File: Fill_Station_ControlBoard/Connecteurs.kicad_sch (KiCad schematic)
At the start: 57 parts, among them J3 USB_C_Receptacle_USB2.0_14P, J4 DE9_Pins, J6 RJ45_Wuerth_7499010211A, U2 USBLC6-2SC6, U3 TCAN337G, U5 LAN8742A

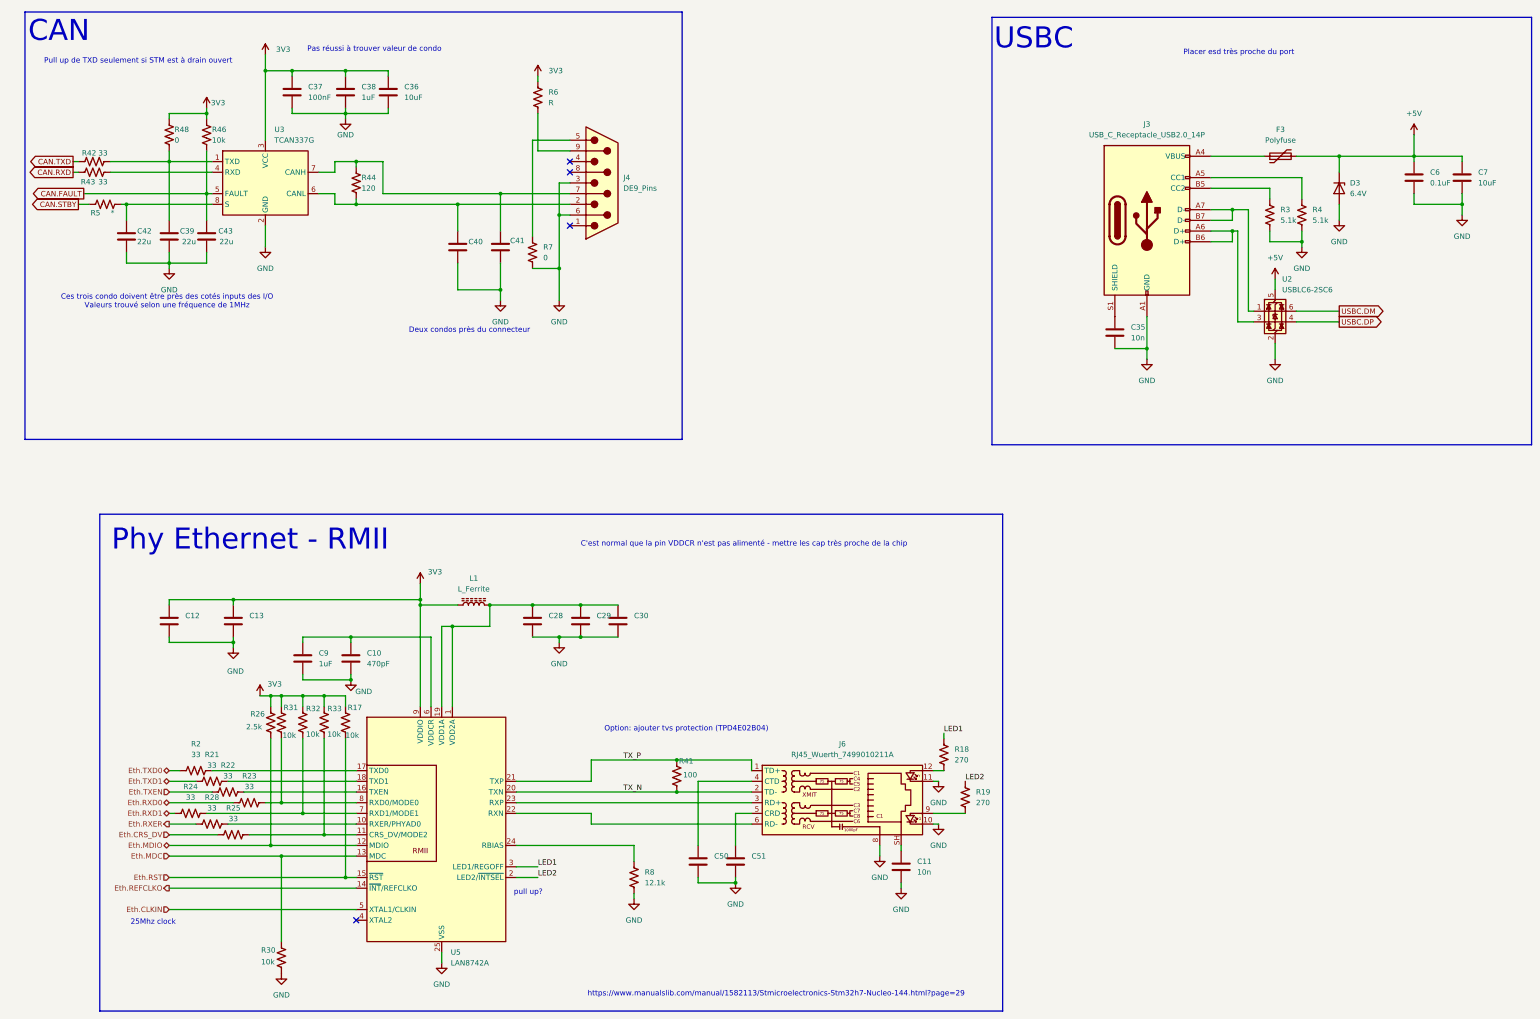
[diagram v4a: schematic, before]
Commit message: Changement de CAN et quelques trucs
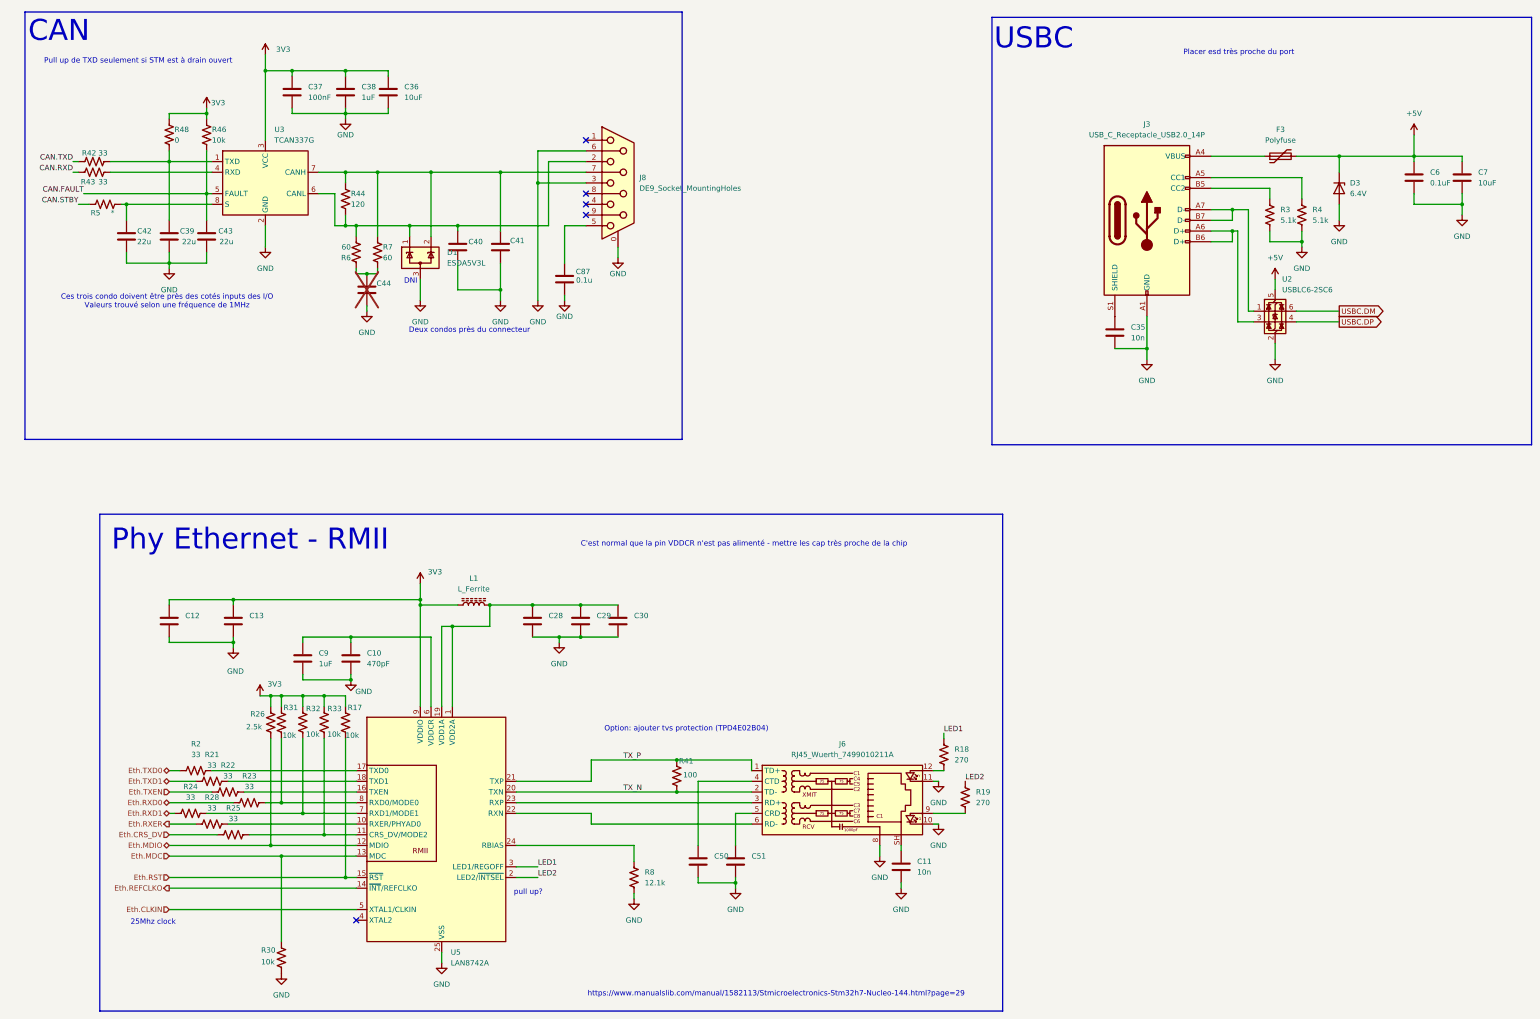
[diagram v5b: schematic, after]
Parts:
- removed J4: DE9_Pins, symbol Connector:DE9_Pins
- added C44: ~, symbol Device:C
- added C87: 0.1u, symbol Device:C
- added D1: ESDA5V3L, Package_TO_SOT_SMD:SOT-23-3, symbol Power_Protection:ESDA5V3L
- added J8: DE9_Socket_MountingHoles, symbol Connector:DE9_Socket_MountingHoles
- R17, R18, R19, R2, R21, R22, R23, R24, R25, R26, R28, R3, R30, R31, R32, R33, R4, R41, R42, R43, R44, R46, R48, R5, R8: footprint (none) -> Resistor_SMD:R_0603_1608Metric_Pad0.98x0.95mm_HandSolder
- R6: value R -> 60; footprint (none) -> Resistor_SMD:R_0603_1608Metric_Pad0.98x0.95mm_HandSolder
- R7: value 0 -> 60; footprint (none) -> Resistor_SMD:R_0603_1608Metric_Pad0.98x0.95mm_HandSolder
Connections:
- net 3V3: no longer R6.1
- net GND: now also C44.2, C87.1, D1.3 (A), J8.0 (PAD), J8.3, J8.6; no longer R7.2
- net at R7.1: now also C41.1, R44.1, U3.7 (CANH), D1.2 (K), J8.7
- net at C40.1, R44.2, U3.6 (CANL): now also R6.2, D1.1 (K), J8.2
- new net: C87.2, J8.5
- new net: C44.1, R6.1, R7.2
- no-connect marks 4 -> 5
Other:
- note added: "DNI"
- note removed: "Pas réussi à trouver valeur de condo"
- moved on the sheet: R44

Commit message: Assignation footprint pis valeurs resistances del
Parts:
- C10, C11, C12, C13, C28, C29, C30, C35, C36, C37, C38, C39, C40, C41, C42, C43, C44, C50, C51, C6, C7, C87, C9: footprint (none) -> Capacitor_SMD:C_0603_1608Metric
- U3: footprint (none) -> Package_TO_SOT_SMD:TSOT-23-8_HandSoldering
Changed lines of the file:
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@@
 			)
 		)
-		(property "Footprint" ""
+		(property "Footprint" "Capacitor_SMD:C_0603_1608Metric"
 			(at 63.1952 175.26 0)
 			(effects
@@
 			)
 		)
-		(property "Footprint" ""
+		(property "Footprint" "Capacitor_SMD:C_0603_1608Metric"
 			(at 157.1752 86.36 0)
 			(effects
@@
 			)
 		)
-		(property "Footprint" ""
+		(property "Footprint" "Capacitor_SMD:C_0603_1608Metric"
 			(at 141.9352 86.36 0)
 			(effects
@@
 			)
 		)
-		(property "Footprint" ""
+		(property "Footprint" "Capacitor_SMD:C_0603_1608Metric"
 			(at 94.9452 184.15 0)
 			(effects
@@
 			)
 		)
-		(property "Footprint" ""
+		(property "Footprint" "Capacitor_SMD:C_0603_1608Metric"
 			(at 92.4052 49.53 0)
 			(effects
@@
 			)
 		)
-		(property "Footprint" ""
+		(property "Footprint" "Capacitor_SMD:C_0603_1608Metric"
 			(at 160.9852 175.26 0)
 			(effects
@@
 			)
 		)
-		(property "Footprint" ""
+		(property "Footprint" "Capacitor_SMD:C_0603_1608Metric"
 			(at 370.5352 69.85 0)
 			(effects
@@
 			)
 		)
-		(property "Footprint" ""
+		(property "Footprint" "Capacitor_SMD:C_0603_1608Metric"
 			(at 63.1952 83.82 0)
 			(effects
@@
 			)
 		)
-		(property "Footprint" ""
+		(property "Footprint" "Package_TO_SOT_SMD:TSOT-23-8_HandSoldering"
 			(at 85.09 80.01 0)
 			(effects
@@
 			)
 		)
-		(property "Footprint" ""
+		(property "Footprint" "Capacitor_SMD:C_0603_1608Metric"
 			(at 197.8152 232.41 0)
 			(effects
@@
 			)
 		)
-		(property "Footprint" ""
+		(property "Footprint" "Capacitor_SMD:C_0603_1608Metric"
 			(at 149.5552 175.26 0)
 			(effects
@@
 			)
 		)
-		(property "Footprint" ""
+		(property "Footprint" "Capacitor_SMD:C_0603_1608Metric"
 			(at 53.0352 83.82 0)
 			(effects
@@
 			)
 		)
-		(property "Footprint" ""
+		(property "Footprint" "Capacitor_SMD:C_0603_1608Metric"
 			(at 359.1052 69.85 0)
 			(effects
@@
 			)
 		)
-		(property "Footprint" ""
+		(property "Footprint" "Capacitor_SMD:C_0603_1608Metric"
 			(at 188.9252 232.41 0)
 			(effects
@@
 			)
 		)
-		(property "Footprint" ""
+		(property "Footprint" "Capacitor_SMD:C_0603_1608Metric"
 			(at 110.1852 96.52 0)
 			(effects
@@
 			)
 		)
-		(property "Footprint" ""
+		(property "Footprint" "Capacitor_SMD:C_0603_1608Metric"
 			(at 237.1852 233.68 0)
 			(effects
@@
 			)
 		)
-		(property "Footprint" ""
+		(property "Footprint" "Capacitor_SMD:C_0603_1608Metric"
 			(at 131.7752 86.36 0)
 			(effects
@@
 			)
 		)
-		(property "Footprint" ""
+		(property "Footprint" "Capacitor_SMD:C_0603_1608Metric"
 			(at 169.8752 175.26 0)
 			(effects
@@
 			)
 		)
-		(property "Footprint" ""
+		(property "Footprint" "Capacitor_SMD:C_0603_1608Metric"
 			(at 78.4352 175.26 0)
 			(effects
@@
 			)
 		)
-		(property "Footprint" ""
+		(property "Footprint" "Capacitor_SMD:C_0603_1608Metric"
 			(at 105.1052 49.53 0)
 			(effects
@@
 			)
 		)
-		(property "Footprint" ""
+		(property "Footprint" "Capacitor_SMD:C_0603_1608Metric"
 			(at 287.9852 106.68 0)
 			(effects
@@
 			)
 		)
-		(property "Footprint" ""
+		(property "Footprint" "Capacitor_SMD:C_0603_1608Metric"
 			(at 72.0852 83.82 0)
 			(effects
@@
 			)
 		)
-		(property "Footprint" ""
+		(property "Footprint" "Capacitor_SMD:C_0603_1608Metric"
 			(at 106.3752 184.15 0)
 			(effects
@@
 			)
 		)
-		(property "Footprint" ""
+		(property "Footprint" "Capacitor_SMD:C_0603_1608Metric"
 			(at 115.2652 49.53 0)
 			(effects

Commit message: Fait des trucs (commencer arrangement de pièces sur PCB
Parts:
- J3: footprint (none) -> Connector_USB:USB_C_Receptacle_Amphenol_12401548E4-2A_CircularHoles
- J8: footprint (none) -> Connector_Dsub:DSUB-9_Socket_Vertical_P2.77x2.84mm_MountingHoles
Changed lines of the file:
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@@
 		)
 	)
-	(label "CAN.STBY"
-		(at 40.64 72.39 180)
-		(effects
-			(font
-				(size 1.27 1.27)
-			)
-			(justify right bottom)
-		)
-	)
-	(label "CAN.RXD"
-		(at 39.37 64.77 180)
-		(effects
-			(font
-				(size 1.27 1.27)
-			)
-			(justify right bottom)
-		)
-	)
 	(label "LED2"
 		(at 149.86 232.41 0)
@@
 		)
 	)
-	(label "CAN.FAULT"
-		(at 41.91 69.85 180)
-		(effects
-			(font
-				(size 1.27 1.27)
-			)
-			(justify right bottom)
-		)
-	)
 	(label "TX_P"
 		(at 170.18 204.47 0)
@@
 		)
 	)
-	(label "CAN.TXD"
-		(at 39.37 62.23 180)
-		(effects
-			(font
-				(size 1.27 1.27)
-			)
-			(justify right bottom)
-		)
-	)
 	(global_label "USBC.DP"
 		(shape output)
@@
 		)
 	)
+	(hierarchical_label "CAN.STBY"
+		(shape input)
+		(at 40.64 72.39 180)
+		(effects
+			(font
+				(size 1.27 1.27)
+			)
+			(justify right)
+		)
+	)
 	(hierarchical_label "Eth.MDC"
 		(shape input)
@@
 		)
 	)
+	(hierarchical_label "CAN.FAULT"
+		(shape output)
+		(at 41.91 69.85 180)
+		(effects
+			(font
+				(size 1.27 1.27)
+			)
+			(justify right)
+		)
+	)
+	(hierarchical_label "CAN.RXD"
+		(shape bidirectional)
+		(at 39.37 64.77 180)
+		(effects
+			(font
+				(size 1.27 1.27)
+			)
+			(justify right)
+		)
+	)
+	(hierarchical_label "CAN.TXD"
+		(shape bidirectional)
+		(at 39.37 62.23 180)
+		(effects
+			(font
+				(size 1.27 1.27)
+			)
+			(justify right)
+		)
+	)
 	(hierarchical_label "Eth.REFCLKO"
 		(shape output)
@@
 			)
 		)
-		(property "Footprint" ""
+		(property "Footprint" "Connector_Dsub:DSUB-9_Socket_Vertical_P2.77x2.84mm_MountingHoles"
 			(at 168.91 67.31 0)
 			(effects
@@
 			)
 		)
-		(property "Footprint" ""
+		(property "Footprint" "Connector_USB:USB_C_Receptacle_Amphenol_12401548E4-2A_CircularHoles"
 			(at 298.45 76.2 0)
 			(effects

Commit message: Vince
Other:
- moved on the sheet: C35
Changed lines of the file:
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@@
 	)
 	(junction
+		(at 294.64 111.76)
+		(diameter 0)
+		(color 0 0 0 0)
+	)
+	(junction
 		(at 104.14 64.77)
 		(diameter 0)
@@
 	)
 	(junction
-		(at 294.64 106.68)
-		(diameter 0)
-		(color 0 0 0 0)
-	)
-	(junction
 		(at 71.12 50.8)
 		(diameter 0)
@@
 	(wire
 		(pts
-			(xy 294.64 99.06) (xy 294.64 106.68)
-		)
-		(stroke
-			(width 0)
-			(type default)
-		)
-	)
-	(wire
-		(pts
-			(xy 294.64 106.68) (xy 294.64 109.22)
-		)
-		(stroke
-			(width 0)
-			(type default)
-		)
-	)
-	(wire
-		(pts
 			(xy 99.06 199.39) (xy 99.06 222.25)
 		)
@@
 	(wire
 		(pts
+			(xy 294.64 111.76) (xy 294.64 113.03)
+		)
+		(stroke
+			(width 0)
+			(type default)
+		)
+	)
+	(wire
+		(pts
 			(xy 106.68 87.63) (xy 106.68 88.9)
 		)
@@
 	(wire
 		(pts
+			(xy 287.02 99.06) (xy 287.02 102.87)
+		)
+		(stroke
+			(width 0)
+			(type default)
+		)
+	)
+	(wire
+		(pts
 			(xy 104.14 40.64) (xy 104.14 41.91)
 		)
@@
 	(wire
 		(pts
-			(xy 287.02 106.68) (xy 294.64 106.68)
+			(xy 287.02 111.76) (xy 294.64 111.76)
 		)
 		(stroke
@@
 	(wire
 		(pts
+			(xy 287.02 111.76) (xy 287.02 110.49)
+		)
+		(stroke
+			(width 0)
+			(type default)
+		)
+	)
+	(wire
+		(pts
 			(xy 62.23 59.69) (xy 62.23 62.23)
 		)
@@
 	(wire
 		(pts
+			(xy 294.64 99.06) (xy 294.64 111.76)
+		)
+		(stroke
+			(width 0)
+			(type default)
+		)
+	)
+	(wire
+		(pts
 			(xy 62.23 207.01) (xy 64.77 207.01)
 		)
@@
 	(symbol
 		(lib_id "power:GND")
-		(at 294.64 109.22 0)
+		(at 294.64 113.03 0)
 		(unit 1)
 		(exclude_from_sim no)
@@
 		(fields_autoplaced yes)
 		(property "Reference" "#PWR014"
-			(at 294.64 115.57 0)
+			(at 294.64 119.38 0)
 			(effects
 				(font
@@
 		)
 		(property "Value" "GND"
-			(at 294.64 114.3 0)
+			(at 294.64 118.11 0)
 			(effects
 				(font
@@
 		)
 		(property "Footprint" ""
-			(at 294.64 109.22 0)
+			(at 294.64 113.03 0)
 			(effects
 				(font
@@
 		)
 		(property "Datasheet" ""
-			(at 294.64 109.22 0)
+			(at 294.64 113.03 0)
 			(effects
 				(font
@@
 		)
 		(property "Description" "Power symbol creates a global label with name \"GND\" , ground"
-			(at 294.64 109.22 0)
+			(at 294.64 113.03 0)
 			(effects
 				(font
@@
 	(symbol
 		(lib_id "Device:C")
-		(at 287.02 102.87 0)
+		(at 287.02 106.68 0)
 		(unit 1)
 		(exclude_from_sim no)
@@
 		(dnp no)
 		(property "Reference" "C35"
-			(at 290.83 101.5999 0)
+			(at 287.274 104.394 0)
 			(effects
 				(font
@@
 		)
 		(property "Value" "10n"
-			(at 290.83 104.1399 0)
+			(at 287.528 108.712 0)
 			(effects
 				(font
@@
 		)
 		(property "Footprint" "Capacitor_SMD:C_0603_1608Metric"
-			(at 287.9852 106.68 0)
+			(at 287.9852 110.49 0)
 			(effects
 				(font
@@
 		)
 		(property "Datasheet" "~"
-			(at 287.02 102.87 0)
+			(at 287.02 106.68 0)
 			(effects
 				(font
@@
 		)
 		(property "Description" "Unpolarized capacitor"
-			(at 287.02 102.87 0)
+			(at 287.02 106.68 0)
 			(effects
 				(font
